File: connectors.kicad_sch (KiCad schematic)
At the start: 26 parts, among them J1 USB_C_Receptacle_USB2.0_14P, J2 Conn_01x02, M1 Motor_Servo, M2 Motor_Servo, Q1 Q_NMOS, Q2 Q_NMOS, U5 LM74502

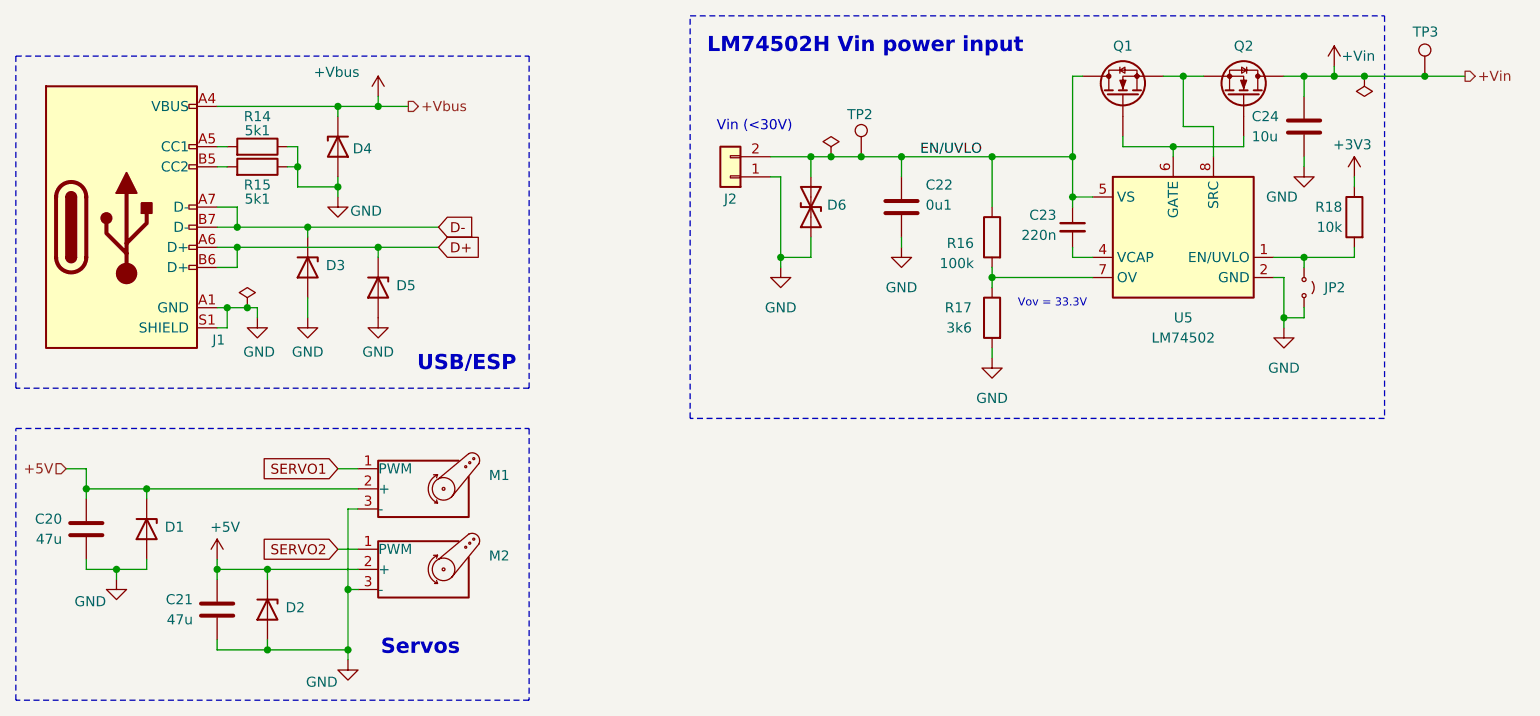
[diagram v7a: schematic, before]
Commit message: schem: renumber
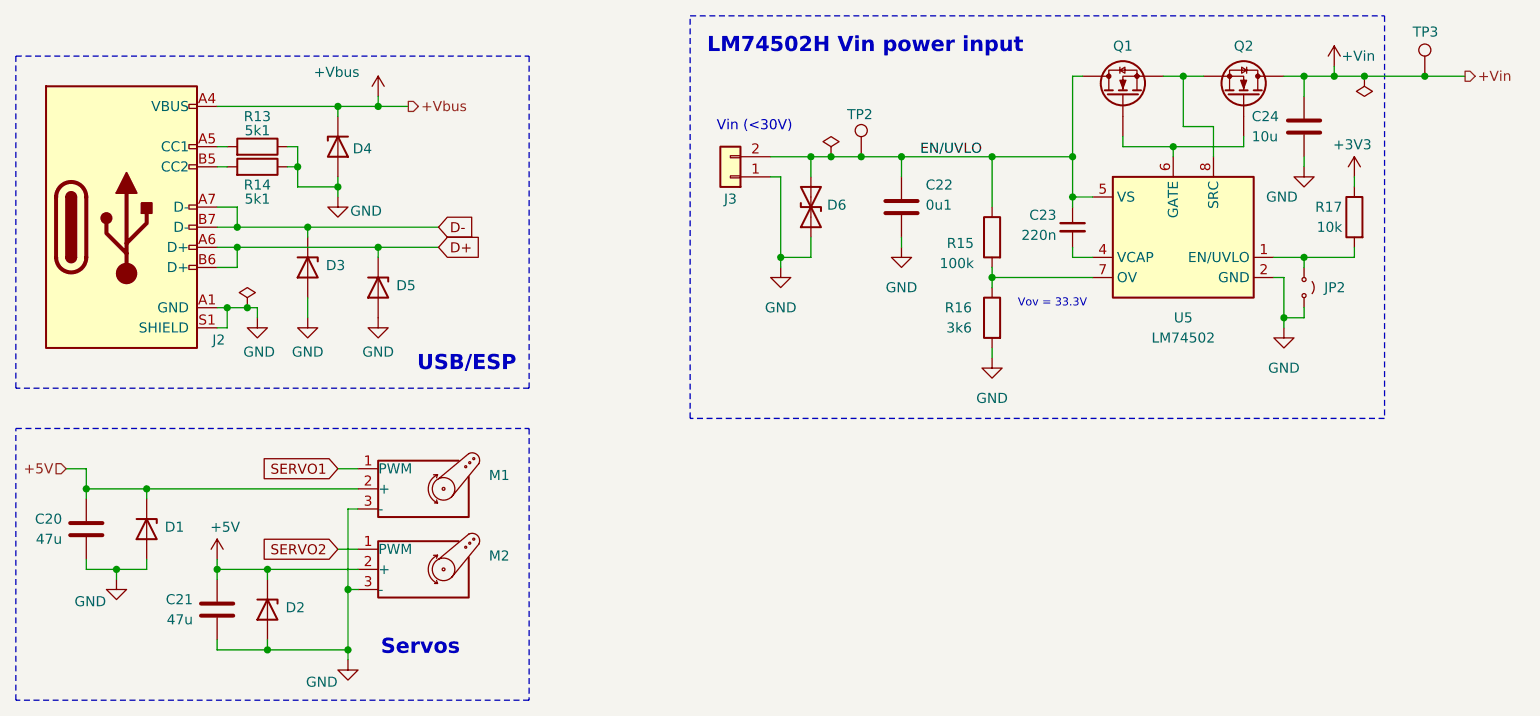
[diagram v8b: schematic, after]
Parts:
- renumbered J1 to J2, J2 to J3, R14 to R13, R15 to R14, R16 to R15, R17 to R16, R18 to R17
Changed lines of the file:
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@@
 		(on_board yes)
 		(dnp no)
-		(property "Reference" "J1"
+		(property "Reference" "J2"
 			(at 88.646 118.364 0)
 			(effects
@@
 			(project "motor-power-poc"
 				(path "/a1dc4c9e-7b20-4b66-a693-9133bc644c6b/dba74ea3-505d-49e4-ba26-48f567962081"
-					(reference "J1")
+					(reference "J2")
 					(unit 1)
 				)
@@
 		(on_board yes)
 		(dnp no)
-		(property "Reference" "#PWR033"
+		(property "Reference" "#PWR035"
 			(at 92.71 121.92 0)
 			(effects
@@
 			(project "motor-power-poc"
 				(path "/a1dc4c9e-7b20-4b66-a693-9133bc644c6b/dba74ea3-505d-49e4-ba26-48f567962081"
-					(reference "#PWR033")
+					(reference "#PWR035")
 					(unit 1)
 				)
@@
 		(on_board yes)
 		(dnp no)
-		(property "Reference" "R15"
+		(property "Reference" "R14"
 			(at 92.71 98.806 90)
 			(effects
@@
 			(project "motor-power-poc"
 				(path "/a1dc4c9e-7b20-4b66-a693-9133bc644c6b/dba74ea3-505d-49e4-ba26-48f567962081"
-					(reference "R15")
+					(reference "R14")
 					(unit 1)
 				)
@@
 		(dnp no)
 		(fields_autoplaced yes)
-		(property "Reference" "#FLG07"
+		(property "Reference" "#FLG04"
 			(at 232.41 86.995 0)
 			(effects
@@
 			(project "motor-power-poc"
 				(path "/a1dc4c9e-7b20-4b66-a693-9133bc644c6b/dba74ea3-505d-49e4-ba26-48f567962081"
-					(reference "#FLG07")
+					(reference "#FLG04")
 					(unit 1)
 				)
@@
 		(on_board yes)
 		(dnp no)
-		(property "Reference" "J2"
+		(property "Reference" "J3"
 			(at 152.4 100.584 0)
 			(effects
@@
 			(project "motor-power-poc"
 				(path "/a1dc4c9e-7b20-4b66-a693-9133bc644c6b/dba74ea3-505d-49e4-ba26-48f567962081"
-					(reference "J2")
+					(reference "J3")
 					(unit 1)
 				)
@@
 		(dnp no)
 		(fields_autoplaced yes)
-		(property "Reference" "#PWR041"
+		(property "Reference" "#PWR043"
 			(at 185.42 127 0)
 			(effects
@@
 			(project "motor-power-poc"
 				(path "/a1dc4c9e-7b20-4b66-a693-9133bc644c6b/dba74ea3-505d-49e4-ba26-48f567962081"
-					(reference "#PWR041")
+					(reference "#PWR043")
 					(unit 1)
 				)
@@
 		(dnp no)
 		(fields_autoplaced yes)
-		(property "Reference" "#PWR039"
+		(property "Reference" "#PWR041"
 			(at 158.75 115.57 0)
 			(effects
@@
 			(project "motor-power-poc"
 				(path "/a1dc4c9e-7b20-4b66-a693-9133bc644c6b/dba74ea3-505d-49e4-ba26-48f567962081"
-					(reference "#PWR039")
+					(reference "#PWR041")
 					(unit 1)
 				)
@@
 		(dnp no)
 		(fields_autoplaced yes)
-		(property "Reference" "#PWR042"
+		(property "Reference" "#PWR044"
 			(at 222.25 123.19 0)
 			(effects
@@
 			(project ""
 				(path "/a1dc4c9e-7b20-4b66-a693-9133bc644c6b/dba74ea3-505d-49e4-ba26-48f567962081"
-					(reference "#PWR042")
+					(reference "#PWR044")
 					(unit 1)
 				)
@@
 		(on_board yes)
 		(dnp no)
-		(property "Reference" "#PWR038"
+		(property "Reference" "#PWR040"
 			(at 107.95 121.92 0)
 			(effects
@@
 			(project "motor-power-poc"
 				(path "/a1dc4c9e-7b20-4b66-a693-9133bc644c6b/dba74ea3-505d-49e4-ba26-48f567962081"
-					(reference "#PWR038")
+					(reference "#PWR040")
 					(unit 1)
 				)
@@
 		(on_board yes)
 		(dnp no)
-		(property "Reference" "R14"
+		(property "Reference" "R13"
 			(at 92.71 90.17 90)
 			(effects
@@
 			(project "motor-power-poc"
 				(path "/a1dc4c9e-7b20-4b66-a693-9133bc644c6b/dba74ea3-505d-49e4-ba26-48f567962081"
-					(reference "R14")
+					(reference "R13")
 					(unit 1)
 				)
@@
 		(dnp no)
 		(fields_autoplaced yes)
-		(property "Reference" "#FLG06"
+		(property "Reference" "#FLG03"
 			(at 165.1 93.345 0)
 			(effects
@@
 			(project "motor-power-poc"
 				(path "/a1dc4c9e-7b20-4b66-a693-9133bc644c6b/dba74ea3-505d-49e4-ba26-48f567962081"
-					(reference "#FLG06")
+					(reference "#FLG03")
 					(unit 1)
 				)
@@
 		(on_board yes)
 		(dnp no)
-		(property "Reference" "#PWR035"
+		(property "Reference" "#PWR037"
 			(at 102.87 106.68 0)
 			(effects
@@
 			(project "motor-power-poc"
 				(path "/a1dc4c9e-7b20-4b66-a693-9133bc644c6b/dba74ea3-505d-49e4-ba26-48f567962081"
-					(reference "#PWR035")
+					(reference "#PWR037")
 					(unit 1)
 				)
@@
 		(on_board yes)
 		(dnp no)
-		(property "Reference" "#PWR031"
+		(property "Reference" "#PWR033"
 			(at 74.93 154.94 0)
 			(effects
@@
 			(project "motor-power-poc"
 				(path "/a1dc4c9e-7b20-4b66-a693-9133bc644c6b/dba74ea3-505d-49e4-ba26-48f567962081"
-					(reference "#PWR031")
+					(reference "#PWR033")
 					(unit 1)
 				)
@@
 		(on_board yes)
 		(dnp no)
-		(property "Reference" "#PWR032"
+		(property "Reference" "#PWR034"
 			(at 87.63 149.86 0)
 			(effects
@@
 			(project "motor-power-poc"
 				(path "/a1dc4c9e-7b20-4b66-a693-9133bc644c6b/dba74ea3-505d-49e4-ba26-48f567962081"
-					(reference "#PWR032")
+					(reference "#PWR034")
 					(unit 1)
 				)
@@
 		(on_board yes)
 		(dnp no)
-		(property "Reference" "#PWR045"
+		(property "Reference" "#PWR047"
 			(at 231.14 101.6 0)
 			(effects
@@
 			(project "motor-power-poc"
 				(path "/a1dc4c9e-7b20-4b66-a693-9133bc644c6b/dba74ea3-505d-49e4-ba26-48f567962081"
-					(reference "#PWR045")
+					(reference "#PWR047")
 					(unit 1)
 				)
@@
 		(on_board yes)
 		(dnp no)
-		(property "Reference" "#PWR043"
+		(property "Reference" "#PWR045"
 			(at 224.79 102.87 0)
 			(effects
@@
 			(project "motor-power-poc"
 				(path "/a1dc4c9e-7b20-4b66-a693-9133bc644c6b/dba74ea3-505d-49e4-ba26-48f567962081"
-					(reference "#PWR043")
+					(reference "#PWR045")
 					(unit 1)
 				)
@@
 		(on_board yes)
 		(dnp no)
-		(property "Reference" "#PWR036"
+		(property "Reference" "#PWR038"
 			(at 104.14 165.1 0)
 			(effects
@@
 			(project ""
 				(path "/a1dc4c9e-7b20-4b66-a693-9133bc644c6b/dba74ea3-505d-49e4-ba26-48f567962081"
-					(reference "#PWR036")
+					(reference "#PWR038")
 					(unit 1)
 				)
@@
 		(dnp no)
 		(fields_autoplaced yes)
-		(property "Reference" "#PWR040"
+		(property "Reference" "#PWR042"
 			(at 173.99 113.03 0)
 			(effects
@@
 			(project "motor-power-poc"
 				(path "/a1dc4c9e-7b20-4b66-a693-9133bc644c6b/dba74ea3-505d-49e4-ba26-48f567962081"
-					(reference "#PWR040")
+					(reference "#PWR042")
 					(unit 1)
 				)
@@
 		(on_board yes)
 		(dnp no)
-		(property "Reference" "#PWR044"
+		(property "Reference" "#PWR046"
 			(at 228.6 87.63 0)
 			(effects
@@
 			(project "motor-power-poc"
 				(path "/a1dc4c9e-7b20-4b66-a693-9133bc644c6b/dba74ea3-505d-49e4-ba26-48f567962081"
-					(reference "#PWR044")
+					(reference "#PWR046")
 					(unit 1)
 				)
@@
 		(on_board yes)
 		(dnp no)
-		(property "Reference" "R17"
+		(property "Reference" "R16"
 			(at 182.88 114.2999 0)
 			(effects
@@
 			(project "motor-power-poc"
 				(path "/a1dc4c9e-7b20-4b66-a693-9133bc644c6b/dba74ea3-505d-49e4-ba26-48f567962081"
-					(reference "R17")
+					(reference "R16")
 					(unit 1)
 				)
@@
 		(on_board yes)
 		(dnp no)
-		(property "Reference" "#PWR037"
+		(property "Reference" "#PWR039"
 			(at 107.95 91.44 0)
 			(effects
@@
 			(project "motor-power-poc"
 				(path "/a1dc4c9e-7b20-4b66-a693-9133bc644c6b/dba74ea3-505d-49e4-ba26-48f567962081"
-					(reference "#PWR037")
+					(reference "#PWR039")
 					(unit 1)
 				)
@@
 		(on_board yes)
 		(dnp no)
-		(property "Reference" "#PWR034"
+		(property "Reference" "#PWR036"
 			(at 99.06 121.92 0)
 			(effects
@@
 			(project "motor-power-poc"
 				(path "/a1dc4c9e-7b20-4b66-a693-9133bc644c6b/dba74ea3-505d-49e4-ba26-48f567962081"
-					(reference "#PWR034")
+					(reference "#PWR036")
 					(unit 1)
 				)
@@
 		(on_board yes)
 		(dnp no)
-		(property "Reference" "R16"
+		(property "Reference" "R15"
 			(at 183.134 106.172 0)
 			(effects
@@
 			(project ""
 				(path "/a1dc4c9e-7b20-4b66-a693-9133bc644c6b/dba74ea3-505d-49e4-ba26-48f567962081"
-					(reference "R16")
+					(reference "R15")
 					(unit 1)
 				)
@@
 		(on_board yes)
 		(dnp no)
-		(property "Reference" "R18"
+		(property "Reference" "R17"
 			(at 229.616 101.6 0)
 			(effects
@@
 			(project "motor-power-poc"
 				(path "/a1dc4c9e-7b20-4b66-a693-9133bc644c6b/dba74ea3-505d-49e4-ba26-48f567962081"
-					(reference "R18")
+					(reference "R17")
 					(unit 1)
 				)
